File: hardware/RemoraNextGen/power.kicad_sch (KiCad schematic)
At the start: 25 parts, among them J1 Track +, J2 Track -, Q1 CSD16327Q3, U1 AP3012, U2 AP2204K-3.3, U3 MCP6002-xSN

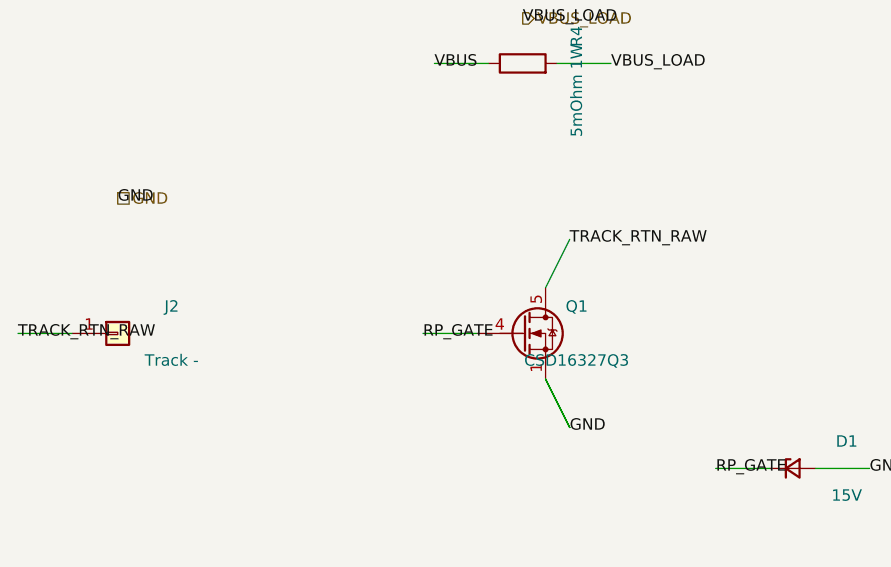
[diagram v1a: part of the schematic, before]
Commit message: Draw real wires instead of floating labels; fix Nucleo lane overlap
Two readability problems, found by actually rendering the generated
schematics to SVG and inspecting them:

- On the root sheet, the 26 Nucleo GPIO/power signals were routed as
  parallel lanes only 4mm apart, each running the full page height.
  ERC was clean, but at any normal zoom they visually merged into an
  unreadable cable bundle. Lanes are now grouped one bundle per
  destination sheet (Power/Motor A/Motor B), with wider in-group
  spacing and a visible gap between groups, sized programmatically
  instead of hardcoded.

- On the power/motor sheets, nearly every net - even between two
  physically adjacent components - was drawn as two disconnected
  stub-wire-and-label islands relying purely on same-name matching,
  never an actual wire. net() now defers to a finalize_nets() pass:
  a net touched at exactly two points gets a real drawn wire (jogged
  if needed); a net touched at 3+ points (GND, VCC, VDD and other
  genuinely pervasive rails) keeps the label convention, matching how
  a real schematic handles shared rails.

Caught a real bug in the first pass at the second fix: a naive
2-segment jog's corner landed exactly on an unrelated VDD hier_label,
silently shorting a motor's current-sense output onto the shared VDD
rail. Fixed by routing jogs through a grid-snapped midpoint instead of
a corner shared with either endpoint's own row/column.

Also ignores *-backups/ (KiCad's own local backup zips).

Co-Authored-By: Claude Sonnet 5 <noreply@anthropic.com>
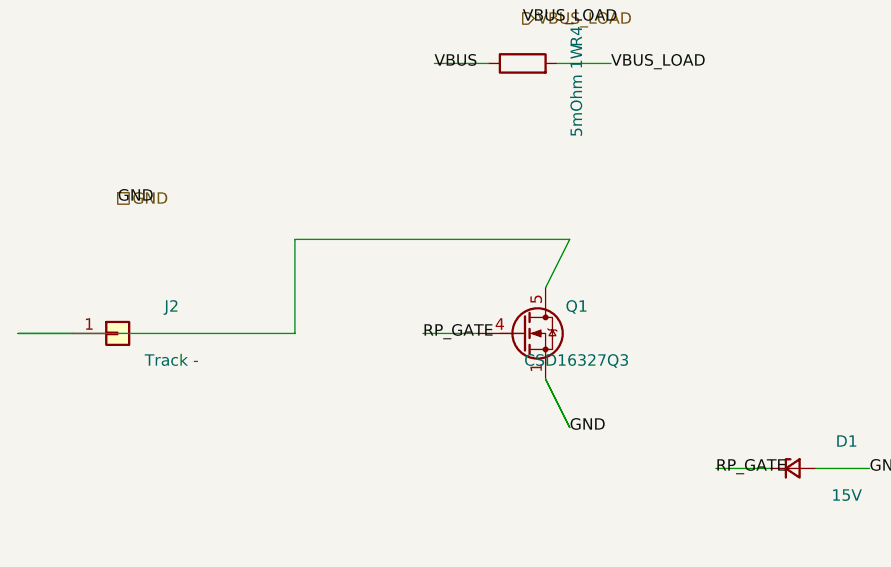
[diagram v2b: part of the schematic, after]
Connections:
- net TRACK_RTN_RAW: no longer names the net of J2.1 (Pin_1), Q1.5 (D)
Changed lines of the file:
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@@
+		(stroke (width 0) (type default))
+	)
+	(wire
+		(pts (xy 28.92 120.00) (xy 59.69 120.00))
+		(stroke (width 0) (type default))
+	)
+	(wire
+		(pts (xy 59.69 120.00) (xy 59.69 109.55))
+		(stroke (width 0) (type default))
+	)
+	(wire
+		(pts (xy 59.69 109.55) (xy 90.22 109.55))
 		(stroke (width 0) (type default))
 	)
@@
 		(effects (font (size 1.27 1.27)))
 	)
+	(label "VBUS"
+		(at 40.00 160.00 0)
+		(effects (font (size 1.27 1.27)))
+	)
 	(label "TRACK_PWR"
 		(at 28.92 160.00 0)
 		(effects (font (size 1.27 1.27)))
 	)
-	(label "TRACK_RTN_RAW"
-		(at 28.92 120.00 0)
-		(effects (font (size 1.27 1.27)))
-	)
 	(label "TRACK_PWR"
 		(at 40.00 175.00 0)
 		(effects (font (size 1.27 1.27)))
 	)
-	(label "TRACK_RTN_RAW"
-		(at 90.22 109.55 0)
+	(label "TRACK_PWR"
+		(at 75.19 155.00 0)
+		(effects (font (size 1.27 1.27)))
+	)
+	(label "TRACK_PWR"
+		(at 40.00 160.00 0)
 		(effects (font (size 1.27 1.27)))
 	)
 	(label "GND"
 		(at 90.22 130.45 0)
+		(effects (font (size 1.27 1.27)))
+	)
+	(label "GND"
+		(at 123.54 135.00 0)
+		(effects (font (size 1.27 1.27)))
+	)
+	(label "GND"
+		(at 160.00 163.62 0)
+		(effects (font (size 1.27 1.27)))
+	)
+	(label "GND"
+		(at 160.00 175.00 0)
+		(effects (font (size 1.27 1.27)))
+	)
+	(label "GND"
+		(at 160.00 190.00 0)
+		(effects (font (size 1.27 1.27)))
+	)
+	(label "GND"
+		(at 169.81 115.00 0)
+		(effects (font (size 1.27 1.27)))
+	)
+	(label "GND"
+		(at 219.81 150.00 0)
+		(effects (font (size 1.27 1.27)))
+	)
+	(label "GND"
+		(at 239.81 130.00 0)
+		(effects (font (size 1.27 1.27)))
+	)
+	(label "GND"
+		(at 260.00 163.62 0)
+		(effects (font (size 1.27 1.27)))
+	)
+	(label "GND"
+		(at 249.81 115.00 0)
+		(effects (font (size 1.27 1.27)))
+	)
+	(label "GND"
+		(at 289.81 115.00 0)
+		(effects (font (size 1.27 1.27)))
+	)
+	(label "GND"
+		(at 339.81 130.00 0)
+		(effects (font (size 1.27 1.27)))
+	)
+	(label "GND"
+		(at 360.56 163.31 0)
+		(effects (font (size 1.27 1.27)))
+	)
+	(label "GND"
+		(at 94.81 40.00 0)
+		(effects (font (size 1.27 1.27)))
+	)
+	(label "GND"
+		(at 40.00 105.00 0)
 		(effects (font (size 1.27 1.27)))
 	)
@@
 		(effects (font (size 1.27 1.27)))
 	)
-	(label "TRACK_PWR"
-		(at 75.19 155.00 0)
-		(effects (font (size 1.27 1.27)))
-	)
 	(label "RP_GATE"
 		(at 94.81 155.00 0)
@@
 		(effects (font (size 1.27 1.27)))
 	)
-	(label "GND"
-		(at 123.54 135.00 0)
-		(effects (font (size 1.27 1.27)))
-	)
-	(label "TRACK_PWR"
-		(at 40.00 160.00 0)
-		(effects (font (size 1.27 1.27)))
-	)
-	(label "VBUS"
-		(at 40.00 160.00 0)
-		(effects (font (size 1.27 1.27)))
-	)
 	(label "VBUS"
 		(at 144.02 146.00 0)
@@
 		(effects (font (size 1.27 1.27)))
 	)
-	(label "GND"
-		(at 160.00 163.62 0)
-		(effects (font (size 1.27 1.27)))
-	)
-	(label "GND"
-		(at 160.00 175.00 0)
-		(effects (font (size 1.27 1.27)))
-	)
-	(label "GND"
-		(at 160.00 190.00 0)
-		(effects (font (size 1.27 1.27)))
-	)
 	(label "VBUS"
 		(at 120.19 165.00 0)
+		(effects (font (size 1.27 1.27)))
+	)
+	(label "VBUS"
+		(at 150.19 115.00 0)
+		(effects (font (size 1.27 1.27)))
+	)
+	(label "VBUS"
+		(at 75.19 90.00 0)
+		(effects (font (size 1.27 1.27)))
+	)
+	(label "VBUS"
+		(at 390.19 165.00 0)
+		(effects (font (size 1.27 1.27)))
+	)
+	(label "VBUS"
+		(at 75.19 60.00 0)
 		(effects (font (size 1.27 1.27)))
 	)
@@
 		(effects (font (size 1.27 1.27)))
 	)
-	(label "VBUS"
-		(at 150.19 115.00 0)
-		(effects (font (size 1.27 1.27)))
-	)
-	(label "GND"
-		(at 169.81 115.00 0)
-		(effects (font (size 1.27 1.27)))
-	)
 	(label "VCC"
 		(at 200.19 150.00 0)
 		(effects (font (size 1.27 1.27)))
 	)
-	(label "GND"
-		(at 219.81 150.00 0)
-		(effects (font (size 1.27 1.27)))
-	)
 	(label "VCC"
 		(at 220.19 165.00 0)
+		(effects (font (size 1.27 1.27)))
+	)
+	(label "VCC"
+		(at 160.00 100.00 0)
+		(effects (font (size 1.27 1.27)))
+	)
+	(label "VCC"
+		(at 160.00 95.00 0)
+		(effects (font (size 1.27 1.27)))
+	)
+	(label "VCC"
+		(at 246.69 145.56 0)
+		(effects (font (size 1.27 1.27)))
+	)
+	(label "VCC"
+		(at 246.38 150.00 0)
+		(effects (font (size 1.27 1.27)))
+	)
+	(label "VCC"
+		(at 230.19 115.00 0)
 		(effects (font (size 1.27 1.27)))
 	)
@@
 		(effects (font (size 1.27 1.27)))
 	)
-	(label "GND"
-		(at 239.81 130.00 0)
-		(effects (font (size 1.27 1.27)))
-	)
-	(label "VCC"
-		(at 160.00 100.00 0)
-		(effects (font (size 1.27 1.27)))
-	)
-	(label "VCC"
-		(at 160.00 95.00 0)
-		(effects (font (size 1.27 1.27)))
-	)
-	(label "VCC"
-		(at 246.69 145.56 0)
-		(effects (font (size 1.27 1.27)))
-	)
-	(label "VCC"
-		(at 246.38 150.00 0)
-		(effects (font (size 1.27 1.27)))
-	)
-	(label "GND"
-		(at 260.00 163.62 0)
-		(effects (font (size 1.27 1.27)))
-	)
 	(label "VDD"
 		(at 273.31 145.56 0)
 		(effects (font (size 1.27 1.27)))
 	)
-	(label "VCC"
-		(at 230.19 115.00 0)
-		(effects (font (size 1.27 1.27)))
-	)
-	(label "GND"
-		(at 249.81 115.00 0)
-		(effects (font (size 1.27 1.27)))
-	)
 	(label "VDD"
 		(at 270.19 115.00 0)
 		(effects (font (size 1.27 1.27)))
 	)
-	(label "GND"
-		(at 289.81 115.00 0)
-		(effects (font (size 1.27 1.27)))
-	)
 	(label "VDD"
 		(at 260.00 95.00 0)
 		(effects (font (size 1.27 1.27)))
 	)
-	(label "VBUS"
-		(at 75.19 90.00 0)
+	(label "VDD"
+		(at 320.19 165.00 0)
+		(effects (font (size 1.27 1.27)))
+	)
+	(label "VDD"
+		(at 360.56 136.69 0)
 		(effects (font (size 1.27 1.27)))
 	)
@@
 		(effects (font (size 1.27 1.27)))
 	)
-	(label "VDD"
-		(at 320.19 165.00 0)
+	(label "VBUS_LOAD"
+		(at 390.19 130.00 0)
 		(effects (font (size 1.27 1.27)))
 	)
@@
 		(effects (font (size 1.27 1.27)))
 	)
-	(label "GND"
-		(at 339.81 130.00 0)
-		(effects (font (size 1.27 1.27)))
-	)
 	(label "VDD_HALF_RAW"
 		(at 351.69 145.56 0)
@@
 		(effects (font (size 1.27 1.27)))
 	)
-	(label "GND"
-		(at 360.56 163.31 0)
-		(effects (font (size 1.27 1.27)))
-	)
-	(label "VDD"
-		(at 360.56 136.69 0)
-		(effects (font (size 1.27 1.27)))
-	)
-	(label "VBUS"
-		(at 390.19 165.00 0)
+	(label "VDD_HALF"
+		(at 454.81 165.00 0)
 		(effects (font (size 1.27 1.27)))
 	)
@@
 		(effects (font (size 1.27 1.27)))
 	)
-	(label "VBUS_LOAD"
-		(at 390.19 130.00 0)
+	(label "DIFF_IN_PLUS"
+		(at 435.19 165.00 0)
 		(effects (font (size 1.27 1.27)))
 	)
@@
 		(effects (font (size 1.27 1.27)))
 	)
-	(label "DIFF_IN_PLUS"
-		(at 435.19 165.00 0)
-		(effects (font (size 1.27 1.27)))
-	)
-	(label "VDD_HALF"
-		(at 454.81 165.00 0)
-		(effects (font (size 1.27 1.27)))
-	)
 	(label "DIFF_IN_MINUS"
 		(at 435.19 130.00 0)
@@
 		(effects (font (size 1.27 1.27)))
 	)
-	(label "VBUS"
-		(at 75.19 60.00 0)
-		(effects (font (size 1.27 1.27)))
-	)
 	(label "PB12"
 		(at 94.81 60.00 0)
@@
 		(effects (font (size 1.27 1.27)))
 	)
-	(label "GND"
-		(at 94.81 40.00 0)
-		(effects (font (size 1.27 1.27)))
-	)
 	(label "PB12"
 		(at 100.00 60.00 0)
 		(effects (font (size 1.27 1.27)))
 	)
-	(label "GND"
-		(at 40.00 105.00 0)
-		(effects (font (size 1.27 1.27)))
-	)

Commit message: Fit sub-sheet blocks on the page; wire local nets in power schematic
Motor B's sheet box ran from y=610 to y=1010, but the A0 landscape root
page is only 841mm tall - it silently overflowed the bottom edge by
169mm. Motor A/B's box heights (400mm) were also far bigger than their
actual pin content needs (~240mm). Tightened both to 260mm and now
compute each sheet's Y position from the previous one's bottom edge
plus a fixed gap, instead of hardcoded absolute numbers, so this can't
drift out of sync with the page again.

finalize_nets() previously only drew a real wire for nets with exactly
2 points, so every net touched at 3+ points - the majority of the
power schematic - stayed as disconnected floating labels. Now any net
whose points stay within a 150mm span gets chained together with real
wire regardless of point count; only genuinely page-wide rails (GND,
VCC, VDD, VBUS, and similarly wide-spanning nets like a motor's phase
node or return net) still fall back to labels, matching how a real
schematic handles shared rails. Verified motor_a/b's wide nets still
correctly fall back to labels rather than turning into a new rats-nest.

ERC still 0 errors throughout.

Also ignores ~*.lck (KiCad's file-open lock markers).

Co-Authored-By: Claude Sonnet 5 <noreply@anthropic.com>
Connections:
- net AP3012_SW is gone; now on net VCC: D2.2 (A), L1.2, U1.1 (SW)
- net DIFF_IN_PLUS is gone; now on an unnamed net: R7.2, R9.1, U3.5 (+)
- net VDD_HALF is gone; now on an unnamed net: R9.2, U3.1, U3.2 (-)
- net VDD_HALF_RAW is gone; now on net VDD: R5.2, R6.1, U3.3 (+)
- net AP3012_FB: no longer names the net of R2.2, R3.1, U1.3 (FB)
- net DIFF_IN_MINUS: no longer names the net of R10.1, R8.2, U3.6 (-)
- net RP_GATE: no longer names the net of D1.1 (K), Q1.4 (G), R1.2
- net TRACK_PWR renamed VBUS
